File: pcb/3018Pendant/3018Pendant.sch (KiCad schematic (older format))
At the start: 10 parts, among them J1 Conn_02x04_Odd_Even, J2 SW 1, J3 GND, J4 Vcc, J5 Encoder 1, J6 SW 2, J7 SW XYZ, U1 Arduino_Pro_Mini

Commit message: update readme
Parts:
- J2, J6: footprint Connector_PinHeader_2.54mm:PinHeader_1x01_P2.54mm_Horizontal -> Connector_PinHeader_2.54mm:PinHeader_1x01_P2.54mm_Vertical
- J5: footprint Connector_PinHeader_2.54mm:PinHeader_1x02_P2.54mm_Horizontal -> Connector_PinHeader_2.54mm:PinHeader_1x02_P2.54mm_Vertical
- J7: footprint Connector_PinHeader_2.54mm:PinHeader_1x03_P2.54mm_Horizontal -> Connector_PinHeader_2.54mm:PinHeader_1x03_P2.54mm_Vertical
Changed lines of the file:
@@
 F 0 "J2" H 8130 2942 50  0000 L CNN
 F 1 "SW 1" H 8130 2851 50  0000 L CNN
-F 2 "Connector_PinHeader_2.54mm:PinHeader_1x01_P2.54mm_Horizontal" H 8050 2900 50  0001 C CNN
+F 2 "Connector_PinHeader_2.54mm:PinHeader_1x01_P2.54mm_Vertical" H 8050 2900 50  0001 C CNN
 F 3 "~" H 8050 2900 50  0001 C CNN
 	1    8050 2900
@@
 F 0 "J6" H 8180 3442 50  0000 L CNN
 F 1 "SW 2" H 8180 3351 50  0000 L CNN
-F 2 "Connector_PinHeader_2.54mm:PinHeader_1x01_P2.54mm_Horizontal" H 8100 3400 50  0001 C CNN
+F 2 "Connector_PinHeader_2.54mm:PinHeader_1x01_P2.54mm_Vertical" H 8100 3400 50  0001 C CNN
 F 3 "~" H 8100 3400 50  0001 C CNN
 	1    8100 3400
@@
 F 0 "J7" V 6522 4280 50  0000 L CNN
 F 1 "SW XYZ" V 6613 4280 50  0000 L CNN
-F 2 "Connector_PinHeader_2.54mm:PinHeader_1x03_P2.54mm_Horizontal" H 6650 4100 50  0001 C CNN
+F 2 "Connector_PinHeader_2.54mm:PinHeader_1x03_P2.54mm_Vertical" H 6650 4100 50  0001 C CNN
 F 3 "~" H 6650 4100 50  0001 C CNN
 	1    6650 4100
@@
 F 0 "J5" V 2912 3244 50  0000 L CNN
 F 1 "Encoder 1" V 2800 3000 50  0000 L CNN
-F 2 "Connector_PinHeader_2.54mm:PinHeader_1x02_P2.54mm_Horizontal" H 2850 3200 50  0001 C CNN
+F 2 "Connector_PinHeader_2.54mm:PinHeader_1x02_P2.54mm_Vertical" H 2850 3200 50  0001 C CNN
 F 3 "~" H 2850 3200 50  0001 C CNN
 	1    2850 3200

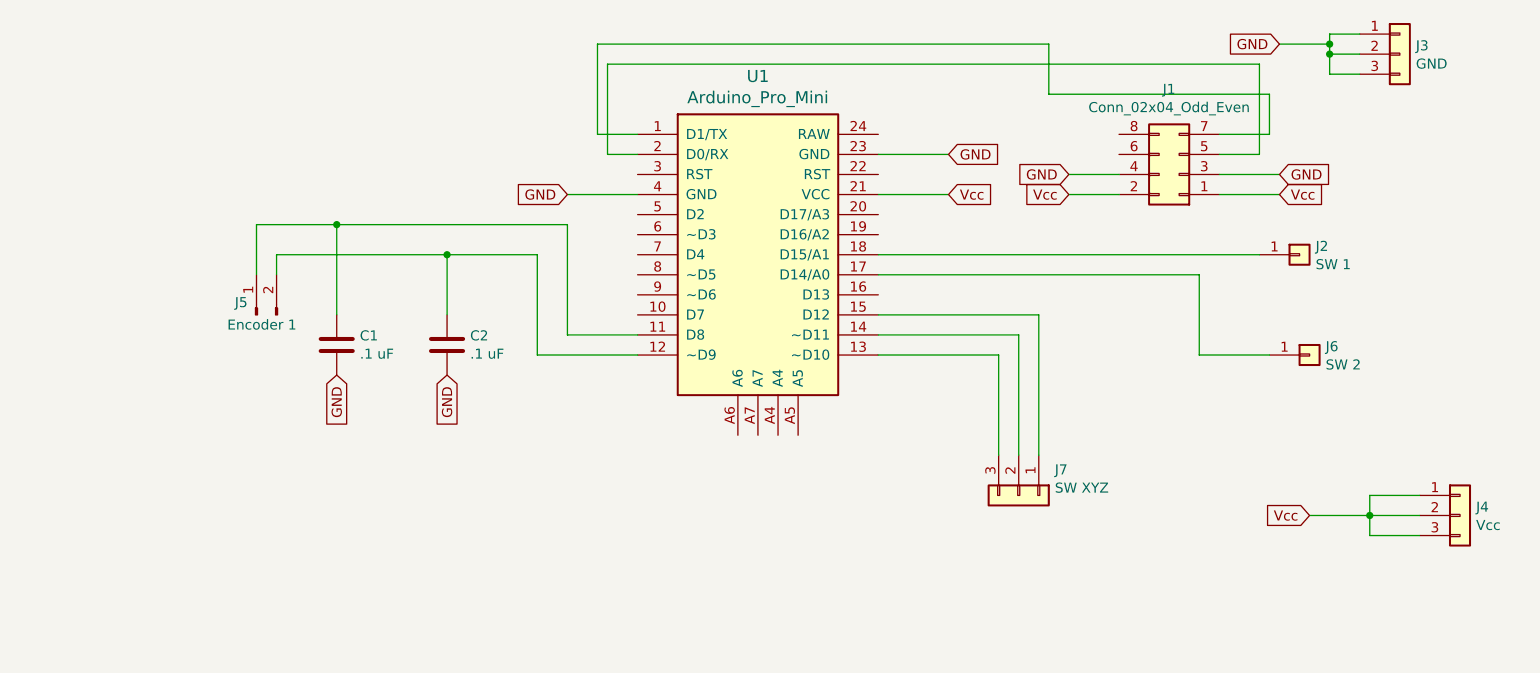
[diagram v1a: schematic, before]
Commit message: Update schematic & PCB to include reset button
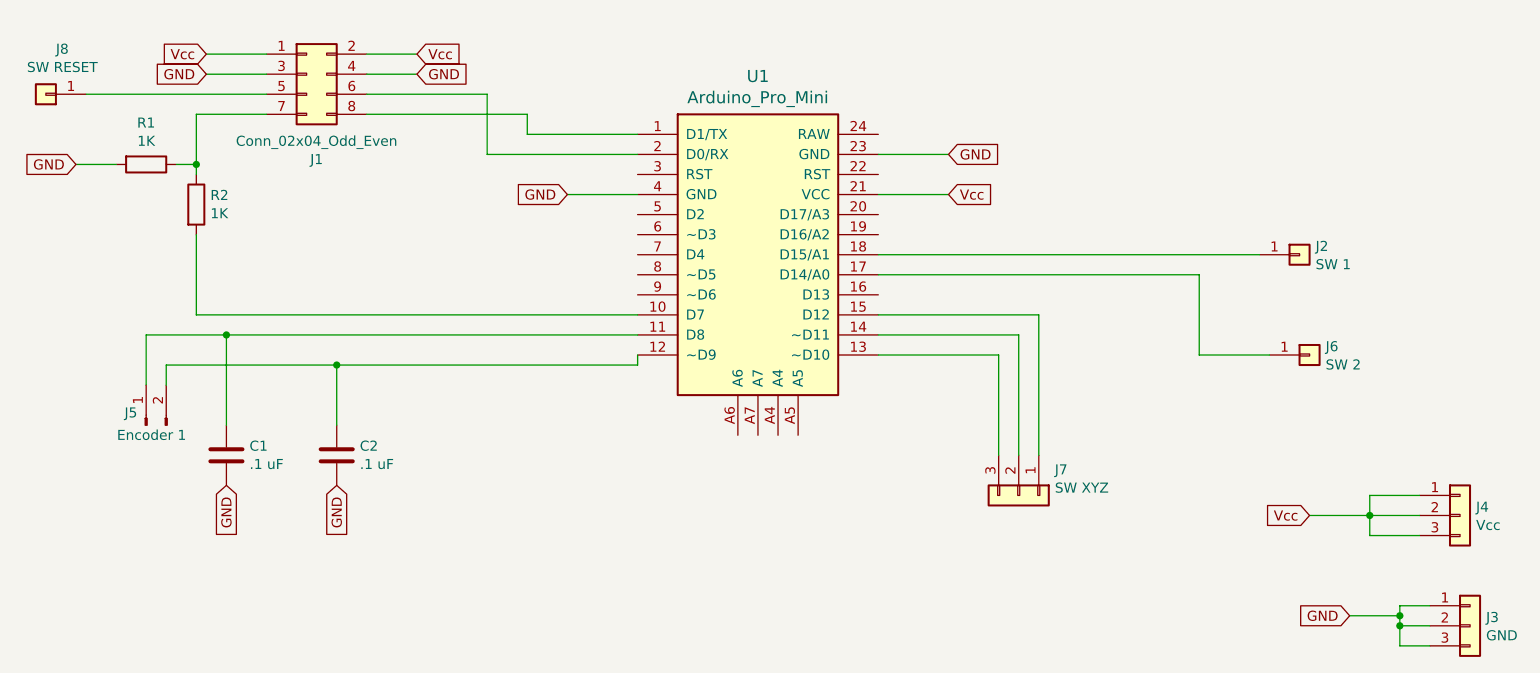
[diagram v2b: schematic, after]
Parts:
- added J8: SW RESET, Connector_PinHeader_2.54mm:PinHeader_1x01_P2.54mm_Vertical, symbol Connector_Generic:Conn_01x01
- added R1, R2: 1K, Resistor_THT:R_Axial_DIN0204_L3.6mm_D1.6mm_P5.08mm_Horizontal, symbol Device:R
- J1: footprint Connector_PinSocket_2.54mm:PinSocket_2x04_P2.54mm_Vertical -> Connector_IDC:IDC-Header_2x04_P2.54mm_Vertical
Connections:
- net GND: now also R1.2
- net at U1.1 (D1/TX): now also J1.8 (Pin_8); no longer J1.7 (Pin_7)
- net at U1.10 (D7): now also R2.2
- net at U1.2 (D0/RX): now also J1.6 (Pin_6); no longer J1.5 (Pin_5)
- new net: J1.5 (Pin_5), J8.1 (Pin_1)
- new net: J1.7 (Pin_7), R1.1, R2.1
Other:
- moved on the sheet: C1, C2, J1, J3, J5
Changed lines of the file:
@@
 	1    0    0    -1
 $EndComp
-$Comp
-L Connector_Generic:Conn_02x04_Odd_Even J1
-U 1 1 61EC90D9
-P 7450 2500
-F 0 "J1" H 7500 2075 50  0000 C CNN
-F 1 "Conn_02x04_Odd_Even" H 7500 2166 50  0000 C CNN
-F 2 "Connector_PinSocket_2.54mm:PinSocket_2x04_P2.54mm_Vertical" H 7450 2500 50  0001 C CNN
-F 3 "~" H 7450 2500 50  0001 C CNN
-	1    7450 2500
-	-1   0    0    1
-$EndComp
-Wire Wire Line
-	4600 1950 4600 2400
-Wire Wire Line
-	4600 2400 4750 2400
-Wire Wire Line
-	6800 1850 4550 1850
-Wire Wire Line
-	4550 1850 4550 2300
-Wire Wire Line
-	4550 2300 4750 2300
 Text GLabel 6300 2600 2    50   Input ~ 0
 Vcc
@@
 GND
 Wire Wire Line
-	5950 2400 6300 2400
-Wire Wire Line
 	5950 2600 6300 2600
-Text GLabel 7950 2600 2    50   Input ~ 0
-Vcc
-Text GLabel 7950 2500 2    50   Input ~ 0
-GND
 $Comp
 L Device:C C2
 U 1 1 61ED484C
-P 3800 3350
-F 0 "C2" H 3915 3396 50  0000 L CNN
-F 1 ".1 uF" H 3915 3305 50  0000 L CNN
-F 2 "Capacitor_THT:C_Axial_L3.8mm_D2.6mm_P7.50mm_Horizontal" H 3838 3200 50  0001 C CNN
-F 3 "~" H 3800 3350 50  0001 C CNN
-	1    3800 3350
+P 3250 3900
+F 0 "C2" H 3365 3946 50  0000 L CNN
+F 1 ".1 uF" H 3365 3855 50  0000 L CNN
+F 2 "Capacitor_THT:C_Axial_L3.8mm_D2.6mm_P7.50mm_Horizontal" H 3288 3750 50  0001 C CNN
+F 3 "~" H 3250 3900 50  0001 C CNN
+	1    3250 3900
 	1    0    0    -1
 $EndComp
@@
 L Device:C C1
 U 1 1 61ED55B8
-P 3250 3350
-F 0 "C1" H 3365 3396 50  0000 L CNN
-F 1 ".1 uF" H 3365 3305 50  0000 L CNN
-F 2 "Capacitor_THT:C_Axial_L3.8mm_D2.6mm_P7.50mm_Horizontal" H 3288 3200 50  0001 C CNN
-F 3 "~" H 3250 3350 50  0001 C CNN
-	1    3250 3350
-	1    0    0    -1
-$EndComp
-Text GLabel 3250 3500 3    50   Input ~ 0
-GND
-Text GLabel 3800 3500 3    50   Input ~ 0
-GND
-Wire Wire Line
-	4400 2750 4400 3300
-Wire Wire Line
-	4400 3300 4750 3300
-Wire Wire Line
-	4250 2900 4250 3400
-Wire Wire Line
-	4250 3400 4750 3400
-Wire Wire Line
-	2950 2900 3800 2900
-Wire Wire Line
-	3250 3200 3250 2750
-Wire Wire Line
-	2850 2750 3250 2750
-Connection ~ 3250 2750
-Wire Wire Line
-	3250 2750 4400 2750
-Connection ~ 3800 2900
-Wire Wire Line
-	3800 2900 4250 2900
+P 2700 3900
+F 0 "C1" H 2815 3946 50  0000 L CNN
+F 1 ".1 uF" H 2815 3855 50  0000 L CNN
+F 2 "Capacitor_THT:C_Axial_L3.8mm_D2.6mm_P7.50mm_Horizontal" H 2738 3750 50  0001 C CNN
+F 3 "~" H 2700 3900 50  0001 C CNN
+	1    2700 3900
+	1    0    0    -1
+$EndComp
+Text GLabel 2700 4050 3    50   Input ~ 0
+GND
+Text GLabel 3250 4050 3    50   Input ~ 0
+GND
+Wire Wire Line
+	2400 3450 3250 3450
+Wire Wire Line
+	2700 3750 2700 3300
+Wire Wire Line
+	2300 3300 2700 3300
+Connection ~ 2700 3300
+Connection ~ 3250 3450
 Wire Wire Line
 	7850 2900 5950 2900
@@
 	6750 3200 5950 3200
 Wire Wire Line
-	3800 2900 3800 3200
+	3250 3450 3250 3750
 $Comp
 L Connector_Generic:Conn_01x03 J3
 U 1 1 61EF795E
-P 8550 1900
-F 0 "J3" H 8630 1942 50  0000 L CNN
-F 1 "GND" H 8630 1851 50  0000 L CNN
-F 2 "Connector_PinHeader_2.54mm:PinHeader_1x03_P2.54mm_Vertical" H 8550 1900 50  0001 C CNN
-F 3 "~" H 8550 1900 50  0001 C CNN
-	1    8550 1900
-	1    0    0    -1
-$EndComp
-Text GLabel 7950 1850 0    50   Input ~ 0
-GND
-Wire Wire Line
-	7950 1850 8200 1850
-Wire Wire Line
-	8200 1850 8200 1800
-Wire Wire Line
-	8200 1800 8350 1800
-Wire Wire Line
-	8350 1900 8200 1900
-Wire Wire Line
-	8200 1900 8200 1850
-Connection ~ 8200 1850
-Wire Wire Line
-	8350 2000 8200 2000
-Wire Wire Line
-	8200 2000 8200 1900
-Connection ~ 8200 1900
+P 8900 4750
+F 0 "J3" H 8980 4792 50  0000 L CNN
+F 1 "GND" H 8980 4701 50  0000 L CNN
+F 2 "Connector_PinHeader_2.54mm:PinHeader_1x03_P2.54mm_Vertical" H 8900 4750 50  0001 C CNN
+F 3 "~" H 8900 4750 50  0001 C CNN
+	1    8900 4750
+	1    0    0    -1
+$EndComp
+Text GLabel 8300 4700 0    50   Input ~ 0
+GND
+Wire Wire Line
+	8300 4700 8550 4700
+Wire Wire Line
+	8550 4700 8550 4650
+Wire Wire Line
+	8550 4650 8700 4650
+Wire Wire Line
+	8700 4750 8550 4750
+Wire Wire Line
+	8550 4750 8550 4700
+Connection ~ 8550 4700
+Wire Wire Line
+	8700 4850 8550 4850
+Wire Wire Line
+	8550 4850 8550 4750
+Connection ~ 8550 4750
 $Comp
 L Connector_Generic:Conn_01x03 J4
@@
 L Connector:Conn_01x02_Male J5
 U 1 1 61F080F7
-P 2850 3200
-F 0 "J5" V 2912 3244 50  0000 L CNN
-F 1 "Encoder 1" V 2800 3000 50  0000 L CNN
-F 2 "Connector_PinHeader_2.54mm:PinHeader_1x02_P2.54mm_Vertical" H 2850 3200 50  0001 C CNN
-F 3 "~" H 2850 3200 50  0001 C CNN
-	1    2850 3200
+P 2300 3750
+F 0 "J5" V 2362 3794 50  0000 L CNN
+F 1 "Encoder 1" V 2250 3550 50  0000 L CNN
+F 2 "Connector_PinHeader_2.54mm:PinHeader_1x02_P2.54mm_Vertical" H 2300 3750 50  0001 C CNN
+F 3 "~" H 2300 3750 50  0001 C CNN
+	1    2300 3750
 	0    -1   -1   0
 $EndComp
 Wire Wire Line
-	2850 2750 2850 3000
-Wire Wire Line
-	2950 2900 2950 3000
-Wire Wire Line
-	7650 2500 7950 2500
-Wire Wire Line
-	7650 2600 7950 2600
-Wire Wire Line
-	6800 1850 6800 2100
-Wire Wire Line
-	6800 2100 7900 2100
-Wire Wire Line
-	7900 2100 7900 2300
-Wire Wire Line
-	7900 2300 7650 2300
-Wire Wire Line
-	7850 1950 7850 2400
-Wire Wire Line
-	7850 2400 7650 2400
-Wire Wire Line
-	4600 1950 7850 1950
-Text GLabel 6900 2500 0    50   Input ~ 0
-GND
-Text GLabel 6900 2600 0    50   Input ~ 0
-Vcc
-Wire Wire Line
-	7150 2500 6900 2500
-Wire Wire Line
-	7150 2600 6900 2600
+	2300 3300 2300 3550
+Wire Wire Line
+	2400 3450 2400 3550
+Wire Wire Line
+	2700 3300 4750 3300
+Wire Wire Line
+	4750 3450 4750 3400
+Wire Wire Line
+	3250 3450 4750 3450
+Wire Wire Line
+	3400 1900 3650 1900
+Wire Wire Line
+	3400 2000 3650 2000
+Text GLabel 3650 1900 2    50   Input ~ 0
+Vcc
+Text GLabel 3650 2000 2    50   Input ~ 0
+GND
+Wire Wire Line
+	2900 1900 2600 1900
+Wire Wire Line
+	2900 2000 2600 2000
+Text GLabel 2600 2000 0    50   Input ~ 0
+GND
+Text GLabel 2600 1900 0    50   Input ~ 0
+Vcc
+$Comp
+L Connector_Generic:Conn_02x04_Odd_Even J1
+U 1 1 61EC90D9
+P 3100 2000
+F 0 "J1" H 3150 1575 50  0000 C CNN
+F 1 "Conn_02x04_Odd_Even" H 3150 1666 50  0000 C CNN
+F 2 "Connector_IDC:IDC-Header_2x04_P2.54mm_Vertical" H 3100 2000 50  0001 C CNN
+F 3 "~" H 3100 2000 50  0001 C CNN
+	1    3100 2000
+	1    0    0    -1
+$EndComp
+Wire Wire Line
+	5950 2400 6300 2400
+Wire Wire Line
+	3400 2100 4000 2100
+Wire Wire Line
+	4000 2100 4000 2400
+Wire Wire Line
+	4000 2400 4750 2400
+Wire Wire Line
+	3400 2200 4200 2200
+Wire Wire Line
+	4200 2200 4200 2300
+Wire Wire Line
+	4200 2300 4750 2300
+$Comp
+L Device:R R2
+U 1 1 61F49319
+P 2550 2650
+F 0 "R2" H 2620 2696 50  0000 L CNN
+F 1 "1K" H 2620 2605 50  0000 L CNN
+F 2 "Resistor_THT:R_Axial_DIN0204_L3.6mm_D1.6mm_P5.08mm_Horizontal" V 2480 2650 50  0001 C CNN
+F 3 "~" H 2550 2650 50  0001 C CNN
+	1    2550 2650
+	1    0    0    -1
+$EndComp
+$Comp
+L Device:R R1
+U 1 1 61F49F79
+P 2300 2450
+F 0 "R1" V 2093 2450 50  0000 C CNN
+F 1 "1K" V 2184 2450 50  0000 C CNN
+F 2 "Resistor_THT:R_Axial_DIN0204_L3.6mm_D1.6mm_P5.08mm_Horizontal" V 2230 2450 50  0001 C CNN
+F 3 "~" H 2300 2450 50  0001 C CNN
+	1    2300 2450
+	0    1    1    0
+$EndComp
+Wire Wire Line
+	2450 2450 2550 2450
+Wire Wire Line
+	2550 2450 2550 2500
+Wire Wire Line
+	2550 2800 2550 3200
+Wire Wire Line
+	2550 3200 4750 3200
+Text GLabel 1950 2450 0    50   Input ~ 0
+GND
+Wire Wire Line
+	2150 2450 1950 2450
+Wire Wire Line
+	2900 2200 2550 2200
+Wire Wire Line
+	2550 2200 2550 2450
+Connection ~ 2550 2450
+$Comp
+L Connector_Generic:Conn_01x01 J8
+U 1 1 61F4ED73
+P 1800 2100
+F 0 "J8" H 1718 1875 50  0000 C CNN
+F 1 "SW RESET" H 1718 1966 50  0000 C CNN
+F 2 "Connector_PinHeader_2.54mm:PinHeader_1x01_P2.54mm_Vertical" H 1800 2100 50  0001 C CNN
+F 3 "~" H 1800 2100 50  0001 C CNN
+	1    1800 2100
+	-1   0    0    1
+$EndComp
+Wire Wire Line
+	2000 2100 2900 2100
 $EndSCHEMATC

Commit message: Add LED
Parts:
- added D1: LED, LED_THT:LED_D3.0mm_Clear, symbol Device:LED
- added R3: 1K, Resistor_THT:R_Axial_DIN0204_L3.6mm_D1.6mm_P5.08mm_Horizontal, symbol Device:R
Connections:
- net GND: now also D1.1 (K)
- net at U1.20 (D17/A3): now also R3.2
- new net: D1.2 (A), R3.1
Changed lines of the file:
@@
 Wire Wire Line
 	2000 2100 2900 2100
+$Comp
+L Device:LED D1
+U 1 1 61F320CA
+P 7150 2700
+F 0 "D1" H 7143 2445 50  0000 C CNN
+F 1 "LED" H 7143 2536 50  0000 C CNN
+F 2 "LED_THT:LED_D3.0mm_Clear" H 7150 2700 50  0001 C CNN
+F 3 "~" H 7150 2700 50  0001 C CNN
+	1    7150 2700
+	-1   0    0    1
+$EndComp
+$Comp
+L Device:R R3
+U 1 1 61F32B62
+P 6850 2700
+F 0 "R3" V 6643 2700 50  0000 C CNN
+F 1 "1K" V 6734 2700 50  0000 C CNN
+F 2 "Resistor_THT:R_Axial_DIN0204_L3.6mm_D1.6mm_P5.08mm_Horizontal" V 6780 2700 50  0001 C CNN
+F 3 "~" H 6850 2700 50  0001 C CNN
+	1    6850 2700
+	0    1    1    0
+$EndComp
+Wire Wire Line
+	5950 2700 6700 2700
+Text GLabel 7450 2700 2    50   Input ~ 0
+GND
+Wire Wire Line
+	7300 2700 7450 2700
 $EndSCHEMATC
